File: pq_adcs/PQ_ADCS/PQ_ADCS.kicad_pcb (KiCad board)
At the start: 4 copper layers, 40 x 40 mm, 51 parts, among them J1 CES-110-02-L-S, J10 Pico-Clasp_01x09, J11 Pico-Clasp_01x15, J12 CES-102-02-L-S, J2 CES-110-02-L-S, J3 CES-110-02-L-S, J4 CES-110-02-L-S, J5 Pico-Clasp_01x03, J6 Pico-Clasp_01x10, J7 Pico-Clasp_01x10, J8 Pico-Clasp_01x10, J9 Pico-Clasp_01x10, U2 LPV542, U3 LPV542, U4 IIM-42652, U5 BD2606MVV, U6 TMUX1108RSVR, U7 MMC5983MA

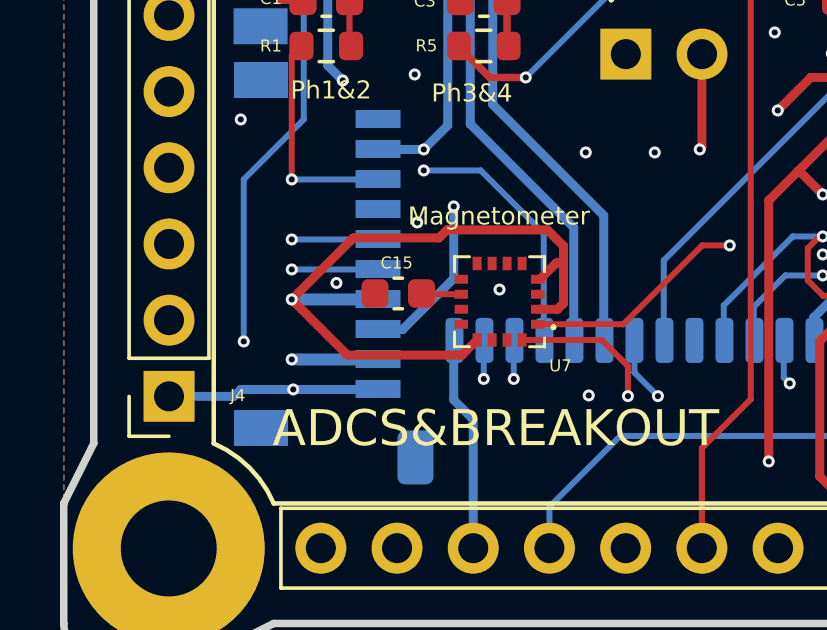
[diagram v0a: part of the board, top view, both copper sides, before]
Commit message: change C15 package from 0603 to 0805
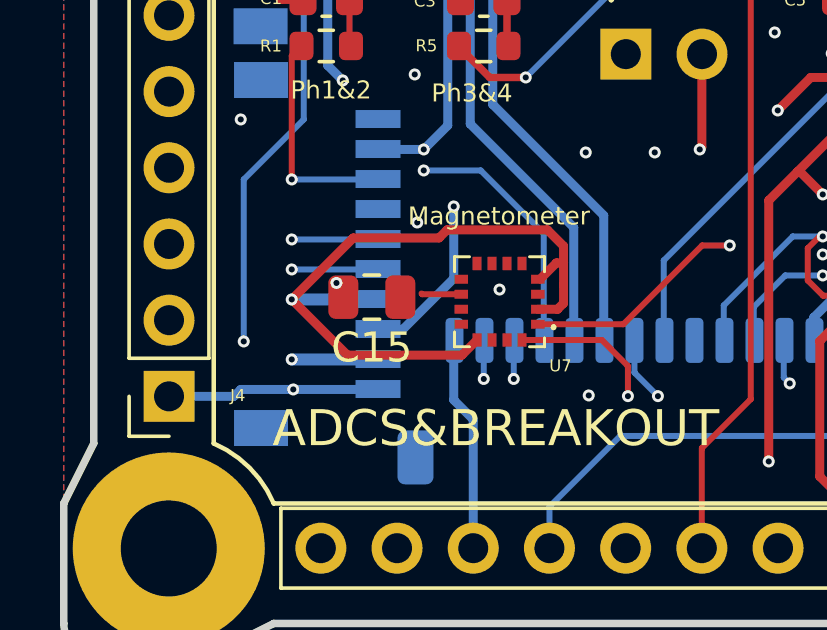
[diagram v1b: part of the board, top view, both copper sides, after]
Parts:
- C15: footprint Capacitor_SMD:C_0603_1608Metric -> Capacitor_SMD:C_0805_2012Metric
- moved C15 0.89 mm to (140.3, 103.1)
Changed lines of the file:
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@@
     )
   )
-  (footprint "Capacitor_SMD:C_0603_1608Metric" (layer "F.Cu")
-    (at 141.15 103 180)
-    (descr "Capacitor SMD 0603 (1608 Metric), square (rectangular) end terminal, IPC_7351 nominal, (Body size source: IPC-SM-782 page 76, https://www.pcb-3d.com/wordpress/wp-content/uploads/ipc-sm-782a_amendment_1_and_2.pdf), generated with kicad-footprint-generator")
+  (footprint "Capacitor_SMD:C_0805_2012Metric" (layer "F.Cu")
+    (at 140.269 103.124 180)
+    (descr "Capacitor SMD 0805 (2012 Metric), square (rectangular) end terminal, IPC_7351 nominal, (Body size source: IPC-SM-782 page 76, https://www.pcb-3d.com/wordpress/wp-content/uploads/ipc-sm-782a_amendment_1_and_2.pdf, https://docs.google.com/spreadsheets/d/1BsfQQcO9C6DZCsRaXUlFlo91Tg2WpOkGARC1WS5S8t0/edit?usp=sharing), generated with kicad-footprint-generator")
     (tags "capacitor")
     (property "Manufacturer 1" "Murata Electronics")
@@
     (property "ki_keywords" "cap capacitor")
     (attr smd)
-    (fp_text reference "C15" (at 0.053 1.019 unlocked) (layer "F.SilkS")
-        (effects (font (size 0.4 0.4) (thickness 0.15)))
-    )
-    (fp_text value "10 uF" (at 0 1.43) (layer "F.Fab")
-        (effects (font (size 1 1) (thickness 0.15)))
-    )
-    (fp_text user "${REFERENCE}" (at 0 0 unlocked) (layer "F.Fab")
-        (effects (font (size 1 1) (thickness 0.15)))
-    )
-    (fp_line (start -0.14058 -0.51) (end 0.14058 -0.51)
-      (stroke (width 0.12) (type solid)) (layer "F.SilkS"))
-    (fp_line (start -0.14058 0.51) (end 0.14058 0.51)
-      (stroke (width 0.12) (type solid)) (layer "F.SilkS"))
-    (fp_line (start -1.48 -0.73) (end 1.48 -0.73)
-      (stroke (width 0.05) (type solid)) (layer "F.CrtYd"))
-    (fp_line (start -1.48 0.73) (end -1.48 -0.73)
-      (stroke (width 0.05) (type solid)) (layer "F.CrtYd"))
-    (fp_line (start 1.48 -0.73) (end 1.48 0.73)
-      (stroke (width 0.05) (type solid)) (layer "F.CrtYd"))
-    (fp_line (start 1.48 0.73) (end -1.48 0.73)
-      (stroke (width 0.05) (type solid)) (layer "F.CrtYd"))
-    (fp_line (start -0.8 -0.4) (end 0.8 -0.4)
-      (stroke (width 0.1) (type solid)) (layer "F.Fab"))
-    (fp_line (start -0.8 0.4) (end -0.8 -0.4)
-      (stroke (width 0.1) (type solid)) (layer "F.Fab"))
-    (fp_line (start 0.8 -0.4) (end 0.8 0.4)
-      (stroke (width 0.1) (type solid)) (layer "F.Fab"))
-    (fp_line (start 0.8 0.4) (end -0.8 0.4)
-      (stroke (width 0.1) (type solid)) (layer "F.Fab"))
-    (pad "1" smd roundrect (at -0.775 0 180) (size 0.9 0.95) (layers "F.Cu" "F.Paste" "F.Mask") (roundrect_rratio 0.25)
+    (fp_text reference "C15" (at 0 -1.68 180) (layer "F.SilkS")
+        (effects (font (size 1 1) (thickness 0.15)))
+    )
+    (fp_text value "10 uF" (at 0 1.68 180) (layer "F.Fab")
+        (effects (font (size 1 1) (thickness 0.15)))
+    )
+    (fp_text user "${REFERENCE}" (at 0 0 180) (layer "F.Fab")
+        (effects (font (size 0.5 0.5) (thickness 0.08)))
+    )
+    (fp_line (start -0.261252 -0.735) (end 0.261252 -0.735)
+      (stroke (width 0.12) (type solid)) (layer "F.SilkS"))
+    (fp_line (start -0.261252 0.735) (end 0.261252 0.735)
+      (stroke (width 0.12) (type solid)) (layer "F.SilkS"))
+    (fp_line (start -1.7 -0.98) (end 1.7 -0.98)
+      (stroke (width 0.05) (type solid)) (layer "F.CrtYd"))
+    (fp_line (start -1.7 0.98) (end -1.7 -0.98)
+      (stroke (width 0.05) (type solid)) (layer "F.CrtYd"))
+    (fp_line (start 1.7 -0.98) (end 1.7 0.98)
+      (stroke (width 0.05) (type solid)) (layer "F.CrtYd"))
+    (fp_line (start 1.7 0.98) (end -1.7 0.98)
+      (stroke (width 0.05) (type solid)) (layer "F.CrtYd"))
+    (fp_line (start -1 -0.625) (end 1 -0.625)
+      (stroke (width 0.1) (type solid)) (layer "F.Fab"))
+    (fp_line (start -1 0.625) (end -1 -0.625)
+      (stroke (width 0.1) (type solid)) (layer "F.Fab"))
+    (fp_line (start 1 -0.625) (end 1 0.625)
+      (stroke (width 0.1) (type solid)) (layer "F.Fab"))
+    (fp_line (start 1 0.625) (end -1 0.625)
+      (stroke (width 0.1) (type solid)) (layer "F.Fab"))
+    (pad "1" smd roundrect (at -0.95 0 180) (size 1 1.45) (layers "F.Cu" "F.Paste" "F.Mask") (roundrect_rratio 0.25)
       (net 75 "Net-(U7-CAP)") (pintype "passive"))
-    (pad "2" smd roundrect (at 0.775 0 180) (size 0.9 0.95) (layers "F.Cu" "F.Paste" "F.Mask") (roundrect_rratio 0.25)
-      (net 1 "GND") (pintype "passive"))
-    (model "${KICAD6_3DMODEL_DIR}/Capacitor_SMD.3dshapes/C_0603_1608Metric.wrl"
+    (pad "2" smd roundrect (at 0.95 0 180) (size 1 1.45) (layers "F.Cu" "F.Paste" "F.Mask") (roundrect_rratio 0.25)
+      (net 1 "GND") (pintype "passive"))
+    (model "${KICAD6_3DMODEL_DIR}/Capacitor_SMD.3dshapes/C_0805_2012Metric.wrl"
       (offset (xyz 0 0 0))
       (scale (xyz 1 1 1))
@@
     (pts (xy 130 76) (xy 170 76.000209))
     (height -10.500193)
-    (gr_text "40.0000 mm" (at 150.000061 64.349912 359.9996992) (layer "Cmts.User")
+    (gr_text "1574,8031 mils" (at 150.000061 64.349912 359.9996992) (layer "Cmts.User")
       (effects (font (size 1 1) (thickness 0.15)))
     )
@@
     (pts (xy 169 115) (xy 169 75))
     (height 14.5)
-    (gr_text "40.0000 mm" (at 182.35 95 90) (layer "Cmts.User")
+    (gr_text "1574,8031 mils" (at 182.35 95 90) (layer "Cmts.User")
       (effects (font (size 1 1) (thickness 0.15)))
     )

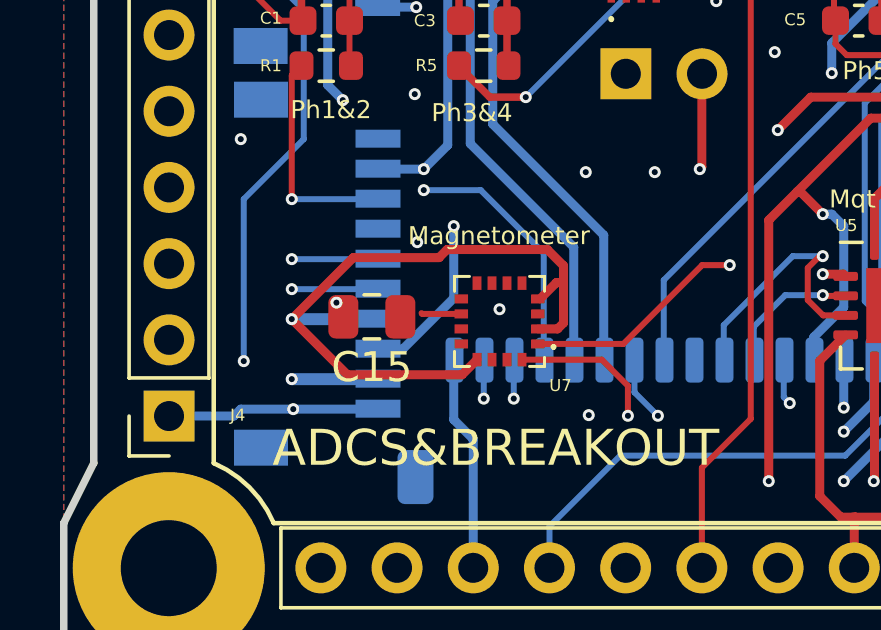
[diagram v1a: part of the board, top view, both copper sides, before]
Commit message: swap SOLARZ with GND
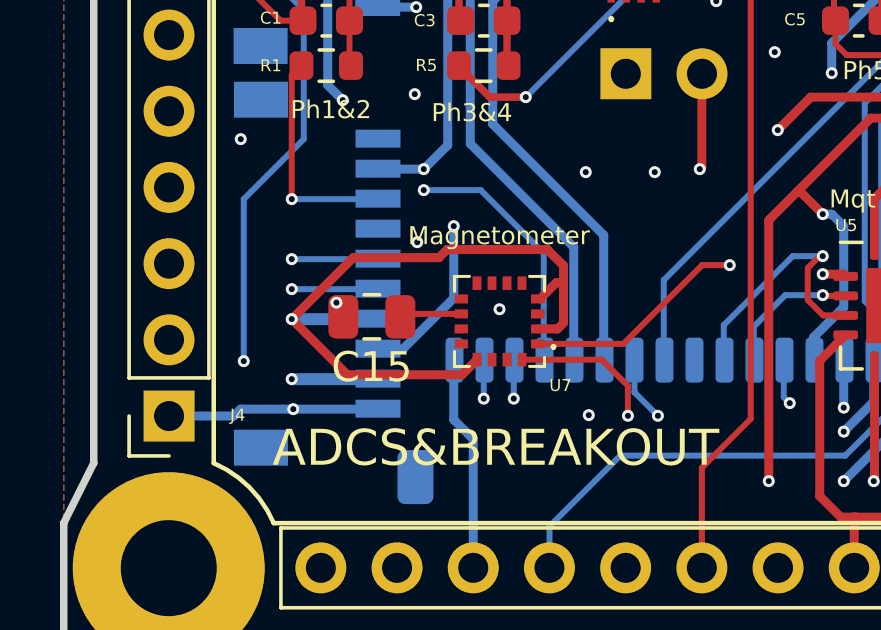
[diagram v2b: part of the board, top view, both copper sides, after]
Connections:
- J2 pad 10: GND -> SOLAR_Z
- J3 pad 1: SOLAR_Z -> GND
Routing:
- net SOLAR_Z: track 63.3 -> 58.5 mm
- net Net-(U7-CAP): track 1.34 -> 2.07 mm
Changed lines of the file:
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@@
       (net 22 "BURNCOMMS") (pinfunction "Pin_9") (pintype "passive"))
     (pad "10" thru_hole oval (at -0.0092 22.86) (size 1.7 1.7) (drill 1) (layers "*.Cu" "*.Mask")
-      (net 1 "GND") (pinfunction "Pin_10") (pintype "passive"))
+      (net 23 "SOLAR_Z") (pinfunction "Pin_10") (pintype "passive"))
     (model "${KICAD_NSL_DIR}/connector-nsl/StepFiles/SLW-110-01-G-S.stp"
       (offset (xyz 0 -11.5 0))
@@
       (stroke (width 0.1) (type solid)) (layer "F.Fab"))
     (pad "1" thru_hole rect (at -0.0092 0 270) (size 1.7 1.7) (drill 1) (layers "*.Cu" "*.Mask")
-      (net 23 "SOLAR_Z") (pinfunction "Pin_1") (pintype "passive"))
+      (net 1 "GND") (pinfunction "Pin_1") (pintype "passive"))
     (pad "2" thru_hole oval (at -0.0092 2.54 270) (size 1.7 1.7) (drill 1) (layers "*.Cu" "*.Mask")
       (net 24 "STM32_PB0") (pinfunction "Pin_2") (pintype "passive"))
@@
     (pts (xy 130 76) (xy 170 76.000209))
     (height -10.500193)
-    (gr_text "1574,8031 mils" (at 150.000061 64.349912 359.9996992) (layer "Cmts.User")
+    (gr_text "40,0000 mm" (at 150.000061 64.349912 359.9996992) (layer "Cmts.User")
       (effects (font (size 1 1) (thickness 0.15)))
     )
@@
     (pts (xy 169 115) (xy 169 75))
     (height 14.5)
-    (gr_text "1574,8031 mils" (at 182.35 95 90) (layer "Cmts.User")
+    (gr_text "40,0000 mm" (at 182.35 95 90) (layer "Cmts.User")
       (effects (font (size 1 1) (thickness 0.15)))
     )
@@
   (via (at 163.4 85.3) (size 0.4) (drill 0.2) (layers "F.Cu" "B.Cu") (net 23))
   (via (at 141.75 92.8) (size 0.4) (drill 0.2) (layers "F.Cu" "B.Cu") (net 23))
+  (segment (start 163.4 85.3) (end 164.45 86.35) (width 0.3) (layer "In2.Cu") (net 23))
   (segment (start 148.875 88.3) (end 141.25 88.3) (width 0.3) (layer "In2.Cu") (net 23))
   (segment (start 140.4 91.45) (end 141.75 92.8) (width 0.3) (layer "In2.Cu") (net 23))
+  (segment (start 164.45 86.35) (end 164.45 105.522) (width 0.3) (layer "In2.Cu") (net 23))
   (segment (start 141.25 88.3) (end 140.4 89.15) (width 0.3) (layer "In2.Cu") (net 23))
   (segment (start 152.875 84.3) (end 148.875 88.3) (width 0.3) (layer "In2.Cu") (net 23))
-  (segment (start 164.45 86.35) (end 164.45 106.2) (width 0.3) (layer "In2.Cu") (net 23))
+  (segment (start 164.45 105.522) (end 165.358 106.43) (width 0.3) (layer "In2.Cu") (net 23))
   (segment (start 140.4 89.15) (end 140.4 91.45) (width 0.3) (layer "In2.Cu") (net 23))
   (segment (start 162.4 84.3) (end 152.875 84.3) (width 0.3) (layer "In2.Cu") (net 23))
-  (segment (start 163.4 85.3) (end 164.45 86.35) (width 0.3) (layer "In2.Cu") (net 23))
-  (segment (start 164.45 106.2) (end 161.43 109.22) (width 0.3) (layer "In2.Cu") (net 23))
-  (segment (start 161.43 109.22) (end 161.43 111.5) (width 0.3) (layer "In2.Cu") (net 23))
+  (segment (start 165.358 106.43) (end 166.4908 106.43) (width 0.3) (layer "In2.Cu") (net 23))
   (segment (start 163.4 85.3) (end 162.4 84.3) (width 0.3) (layer "In2.Cu") (net 23))
   (segment (start 161.9 83.8) (end 159.68 83.8) (width 0.3) (layer "B.Cu") (net 23))
@@
   (segment (start 158.325 105.8162) (end 158.325 104.6875) (width 0.25) (layer "F.Cu") (net 65))
   (segment (start 158.6308 106.122) (end 158.325 105.8162) (width 0.25) (layer "F.Cu") (net 65))
-  (segment (start 143.251 103.0264) (end 141.9514 103.0264) (width 0.2) (layer "F.Cu") (net 75))
-  (segment (start 141.9514 103.0264) (end 141.925 103) (width 0.2) (layer "F.Cu") (net 75))
+  (segment (start 141.3166 103.0264) (end 141.219 103.124) (width 0.2) (layer "F.Cu") (net 75))
+  (segment (start 143.251 103.0264) (end 141.3166 103.0264) (width 0.2) (layer "F.Cu") (net 75))
   (via (at 149.8058 106.422) (size 0.4) (drill 0.2) (layers "F.Cu" "B.Cu") (net 76))
   (segment (start 152.812 104.2068) (end 161.512 104.2068) (width 0.2) (layer "In1.Cu") (net 76))

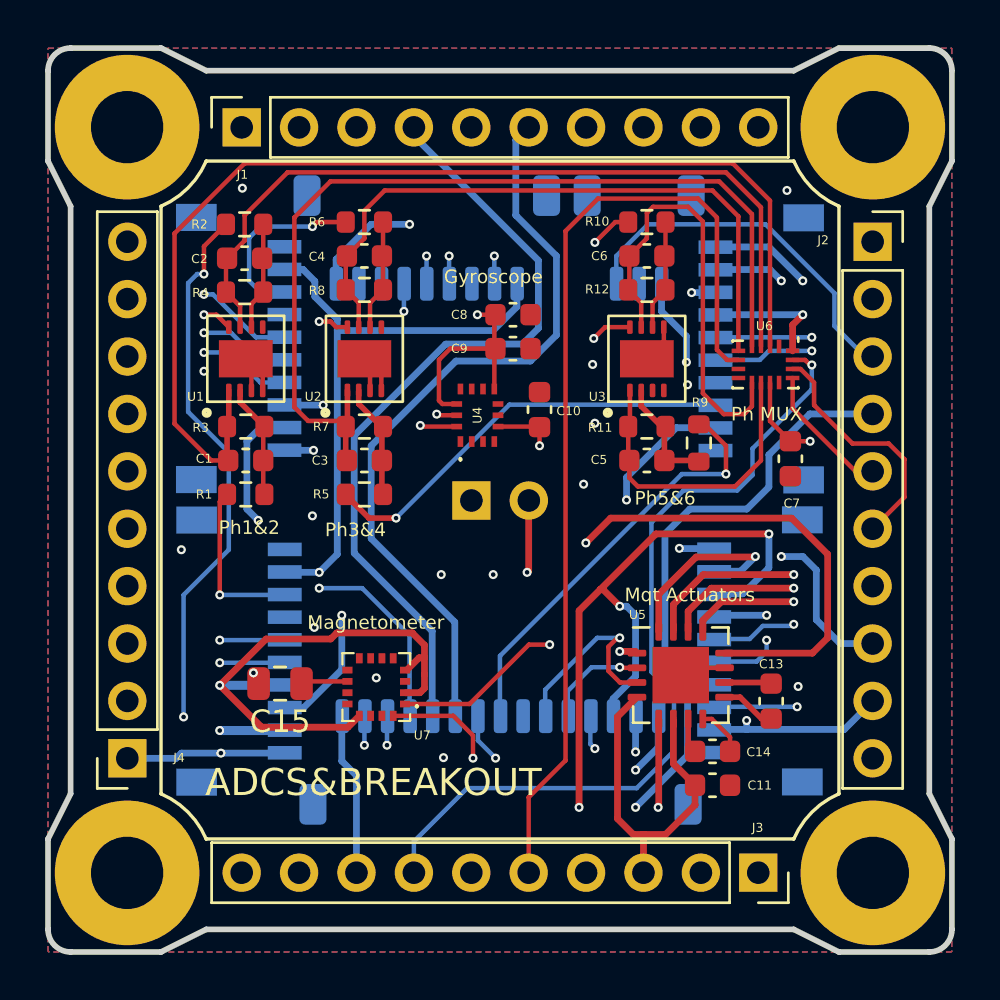
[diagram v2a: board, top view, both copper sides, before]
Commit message: change pin RST_DRIVERS to STM32_PA9, swap SCL3 with NC and redirect all IC to new SCL3 location. Change NC pin to PH_PL, substitute PHT6 to PH_PL and small fixes
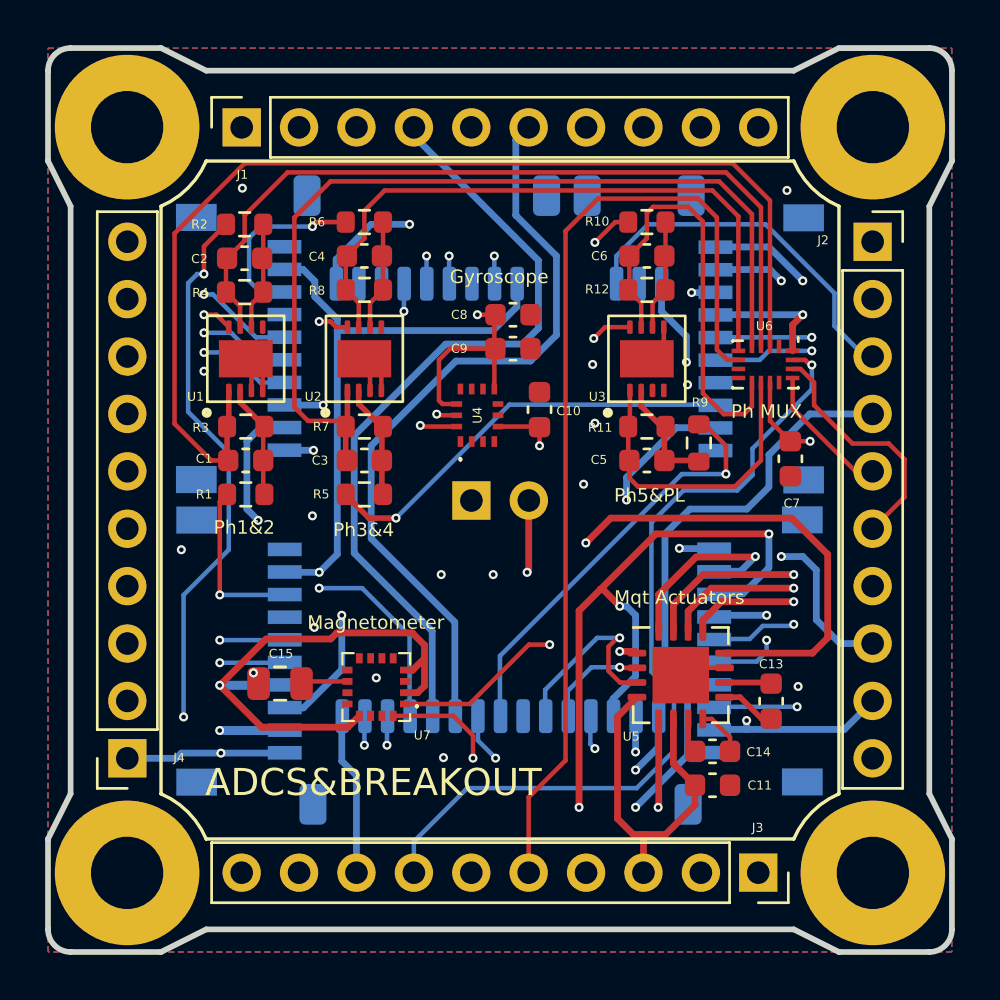
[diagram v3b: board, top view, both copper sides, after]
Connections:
- J1 pad 7: NC -> SCL3
- J10 pad 8: /PHT6 -> PH_PL
- J4 pad 10: SCL3 -> PH_PL
- R10 pad 1: /PHT6 -> PH_PL
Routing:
- net PH_PL: track 0.00 -> 28.4 mm, vias 0 -> 2
- net /PHT6: track 7.62 -> 0.00 mm, vias 2 -> 0
- net SCL3: track 121.1 -> 123.7 mm
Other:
- board text added: "NTC & HEATER"
- board text added: "Ph5&PL"
- board text removed: "BATT"
- board text removed: "Ph5&6"

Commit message: recover the 6 layers ADCS from older versions
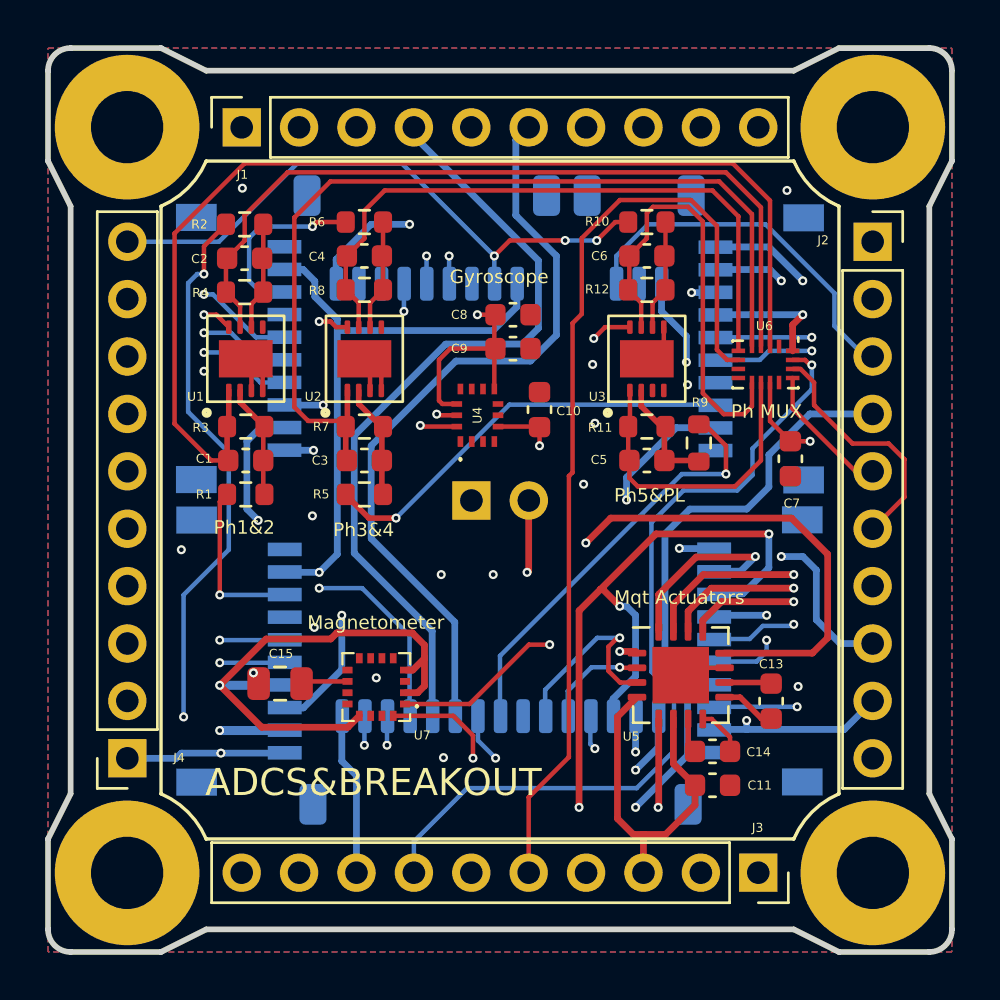
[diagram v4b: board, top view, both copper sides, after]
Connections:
- net RST_DRIVERS renamed STM32_PA9
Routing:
- net PH_PL: track 28.4 -> 27.2 mm, vias 2 -> 3
- net ADC_PH: track 43.7 -> 42.8 mm
- added copper zone on In4.Cu, net GND
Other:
- copper layers 4 -> 6
